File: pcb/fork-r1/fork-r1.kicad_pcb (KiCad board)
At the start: 2 copper layers, 70.1 x 55 mm, 80 parts, among them J1 Bus, J2 Prog, J4 Micro_SD_Card_Det1, J5 VGA, U1 ICE40UP5K-SG48ITR50, U10 MIC5504-3.3YM5, U2 74AHC00PW, U3 SN74CBTD3861PWR, U4 74CBTLV3126PW,118, U5 74LVC4245APW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

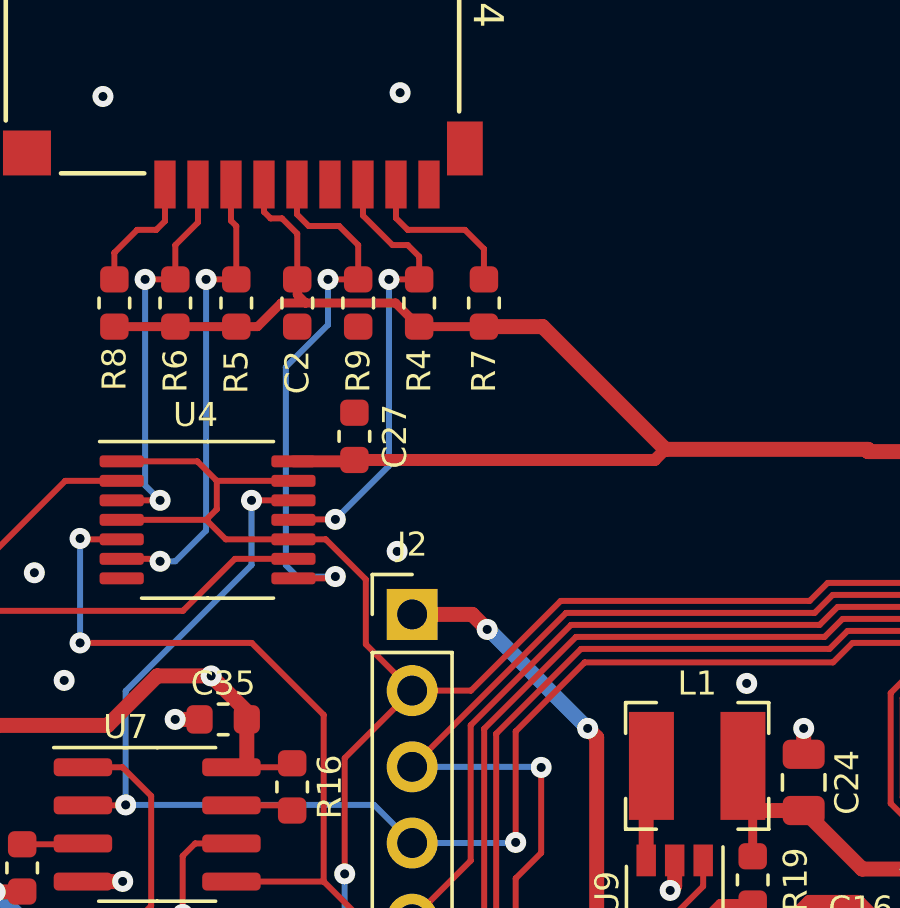
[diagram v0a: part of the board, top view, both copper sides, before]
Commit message: Adding component IDs
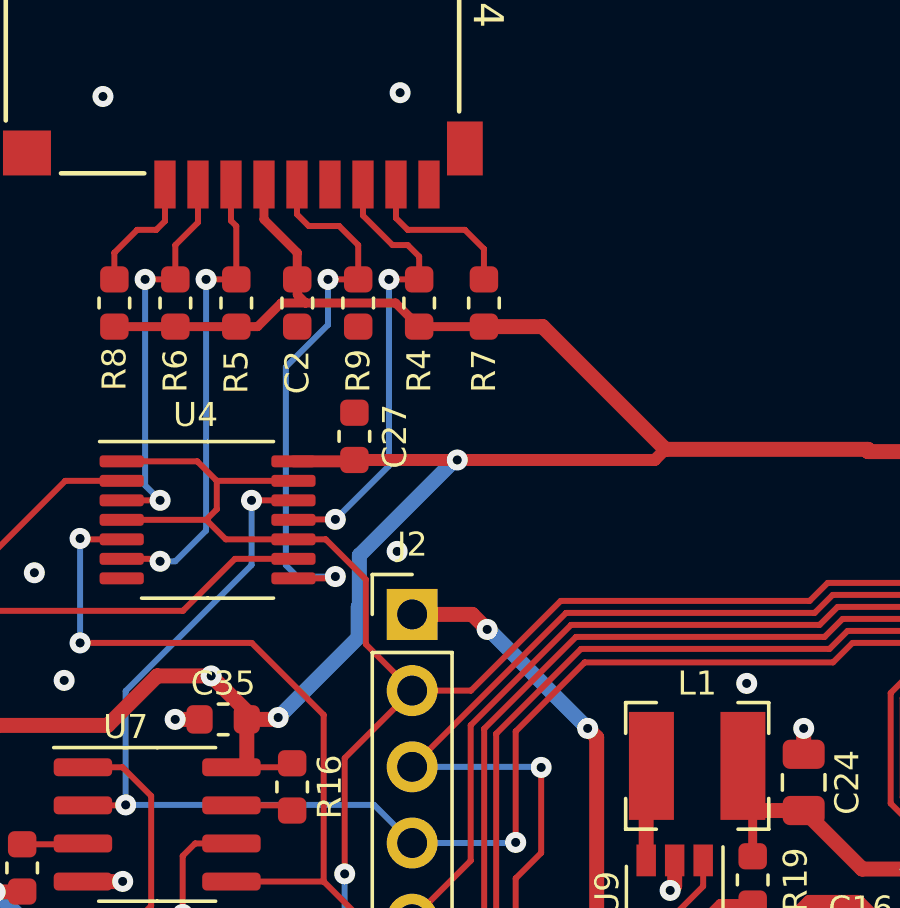
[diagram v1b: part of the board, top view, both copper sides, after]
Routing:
- net +3V3: track 226.7 -> 238.6 mm, vias 18 -> 20

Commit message: Improving R1
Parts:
- H1, H2, H3, H4: footprint MountingHole:MountingHole_3.2mm_M3 -> MountingHole:MountingHole_3.2mm_M3_Pad_Via
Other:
- board text added: "5V"
- board text added: "CDONE"
- board text added: "GND"
- board text added: "MISO"
- board text added: "MOSI"
- board text added: "SCK"
- board text added: "~{RES}"
- board text added: "~{SSEL}"
